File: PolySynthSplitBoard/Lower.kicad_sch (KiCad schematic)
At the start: 3 parts, among them J901 A_LOWER, J902 B_LOWER, J903 C_LOWER

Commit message: lower board
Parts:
- added J904: D_LOWER, Connector_PinSocket_2.54mm:PinSocket_1x03_P2.54mm_Vertical, symbol Connector:Conn_01x03_Pin
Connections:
- net GND: now also J904.1 (Pin_1)
- new net VOL_A: J904.2 (Pin_2)
- new net VOL_W: J904.3 (Pin_3)
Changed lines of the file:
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@@
+	(wire
+		(pts
+			(xy 148.59 127.508) (xy 145.542 127.508)
+		)
+		(stroke
+			(width 0)
+			(type default)
+		)
+	)
 	(wire
 		(pts
@@
 	(wire
 		(pts
+			(xy 148.59 128.524) (xy 148.59 127.508)
+		)
+		(stroke
+			(width 0)
+			(type default)
+		)
+	)
+	(wire
+		(pts
+			(xy 145.034 131.064) (xy 148.59 131.064)
+		)
+		(stroke
+			(width 0)
+			(type default)
+		)
+	)
+	(wire
+		(pts
 			(xy 85.852 131.064) (xy 85.852 130.048)
 		)
@@
 		(pts
 			(xy 84.582 146.304) (xy 85.852 146.304)
+		)
+		(stroke
+			(width 0)
+			(type default)
+		)
+	)
+	(wire
+		(pts
+			(xy 145.034 133.604) (xy 148.59 133.604)
 		)
 		(stroke
@@
 	(rectangle
 		(start 24.384 113.538)
-		(end 137.414 159.258)
+		(end 163.322 159.258)
 		(stroke
 			(width 0)
@@
 		)
 	)
+	(global_label "VOL_A"
+		(shape input)
+		(at 145.034 131.064 180)
+		(fields_autoplaced yes)
+		(effects
+			(font
+				(size 1.27 1.27)
+			)
+			(justify right)
+		)
+		(property "Intersheetrefs" "${INTERSHEET_REFS}"
+			(at 136.5454 131.064 0)
+			(effects
+				(font
+					(size 1.27 1.27)
+				)
+				(justify right)
+				(hide yes)
+			)
+		)
+	)
 	(global_label "EXP_MOSI"
 		(shape input)
@@
 		(property "Intersheetrefs" "${INTERSHEET_REFS}"
 			(at 71.4368 146.304 0)
+			(effects
+				(font
+					(size 1.27 1.27)
+				)
+				(justify right)
+				(hide yes)
+			)
+		)
+	)
+	(global_label "VOL_W"
+		(shape input)
+		(at 145.034 133.604 180)
+		(fields_autoplaced yes)
+		(effects
+			(font
+				(size 1.27 1.27)
+			)
+			(justify right)
+		)
+		(property "Intersheetrefs" "${INTERSHEET_REFS}"
+			(at 136.1826 133.604 0)
 			(effects
 				(font
@@
 				(path "/22649217-9810-470f-bc7b-6f743ad2b90e/3d9ecb3b-9556-42d6-955a-a32d9efd5d3a"
 					(reference "#PWR0902")
+					(unit 1)
+				)
+			)
+		)
+	)
+	(symbol
+		(lib_id "Connector:Conn_01x03_Pin")
+		(at 153.67 131.064 0)
+		(mirror y)
+		(unit 1)
+		(exclude_from_sim no)
+		(in_bom yes)
+		(on_board yes)
+		(dnp no)
+		(property "Reference" "J904"
+			(at 153.035 123.19 0)
+			(effects
+				(font
+					(size 1.27 1.27)
+				)
+			)
+		)
+		(property "Value" "D_LOWER"
+			(at 153.035 125.73 0)
+			(effects
+				(font
+					(size 1.27 1.27)
+				)
+			)
+		)
+		(property "Footprint" "Connector_PinSocket_2.54mm:PinSocket_1x03_P2.54mm_Vertical"
+			(at 153.67 131.064 0)
+			(effects
+				(font
+					(size 1.27 1.27)
+				)
+				(hide yes)
+			)
+		)
+		(property "Datasheet" "~"
+			(at 153.67 131.064 0)
+			(effects
+				(font
+					(size 1.27 1.27)
+				)
+				(hide yes)
+			)
+		)
+		(property "Description" "Generic connector, single row, 01x03, script generated"
+			(at 153.67 131.064 0)
+			(effects
+				(font
+					(size 1.27 1.27)
+				)
+				(hide yes)
+			)
+		)
+		(pin "2"
+		)
+		(pin "1"
+		)
+		(pin "3"
+		)
+		(instances
+			(project ""
+				(path "/22649217-9810-470f-bc7b-6f743ad2b90e/3d9ecb3b-9556-42d6-955a-a32d9efd5d3a"
+					(reference "J904")
 					(unit 1)
 				)
@@
 					(unit 1)
 				)
+			)
+		)
+	)
+	(symbol
+		(lib_id "power:GND")
+		(at 145.542 127.508 0)
+		(unit 1)
+		(exclude_from_sim no)
+		(in_bom yes)
+		(on_board yes)
+		(dnp no)
+		(fields_autoplaced yes)
+		(property "Reference" "#PWR0907"
+			(at 145.542 133.858 0)
+			(effects
+				(font
+					(size 1.27 1.27)
+				)
+				(hide yes)
+			)
+		)
+		(property "Value" "GND"
+			(at 145.542 131.318 0)
+			(effects
+				(font
+					(size 1.27 1.27)
+				)
+				(hide yes)
+			)
+		)
+		(property "Footprint" ""
+			(at 145.542 127.508 0)
+			(effects
+				(font
+					(size 1.27 1.27)
+				)
+				(hide yes)
+			)
+		)
+		(property "Datasheet" ""
+			(at 145.542 127.508 0)
+			(effects
+				(font
+					(size 1.27 1.27)
+				)
+				(hide yes)
+			)
+		)
+		(property "Description" ""
+			(at 145.542 127.508 0)
+			(effects
+				(font
+					(size 1.27 1.27)
+				)
+				(hide yes)
+			)
+		)
+		(pin "1"
+		)
+		(instances
+			(project "PolySynthSplitBoard"
+				(path "/22649217-9810-470f-bc7b-6f743ad2b90e/3d9ecb3b-9556-42d6-955a-a32d9efd5d3a"
+					(reference "#PWR0907")
+					(unit 1)
+				)

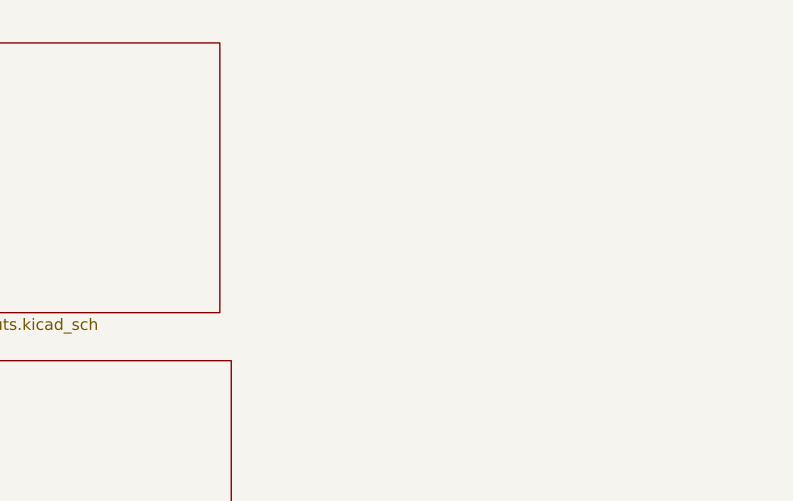
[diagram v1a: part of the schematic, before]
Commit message: hardware chip select for pitch registers
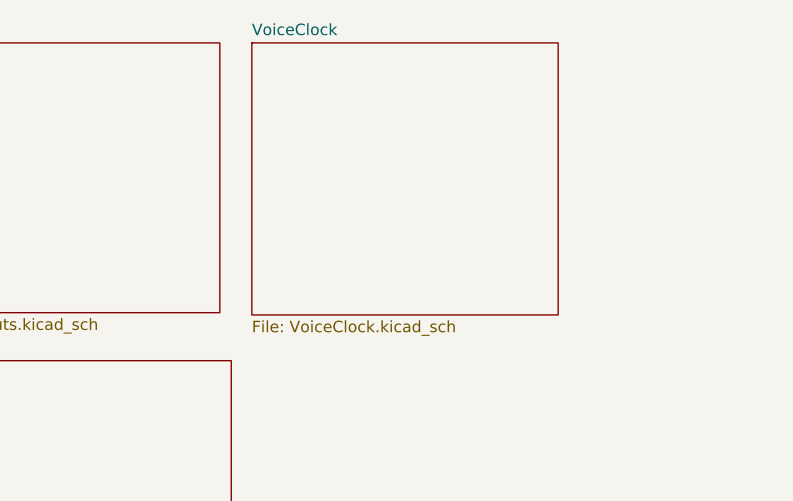
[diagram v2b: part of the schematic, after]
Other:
- added sheet VoiceClock (VoiceClock.kicad_sch)
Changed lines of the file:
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@@
+	)
+	(sheet
+		(at 105.156 22.606)
+		(size 34.036 30.226)
+		(fields_autoplaced yes)
+		(stroke
+			(width 0.1524)
+			(type solid)
+		)
+		(fill
+			(color 0 0 0 0.0000)
+		)
+		(property "Sheetname" "VoiceClock"
+			(at 105.156 21.8944 0)
+			(effects
+				(font
+					(size 1.27 1.27)
+				)
+				(justify left bottom)
+			)
+		)
+		(property "Sheetfile" "VoiceClock.kicad_sch"
+			(at 105.156 53.4166 0)
+			(effects
+				(font
+					(size 1.27 1.27)
+				)
+				(justify left top)
+			)
+		)
+		(instances
+			(project "PolySynthSplitBoard"
+				(path "/22649217-9810-470f-bc7b-6f743ad2b90e/3d9ecb3b-9556-42d6-955a-a32d9efd5d3a"
+					(page "10")
+				)
+			)
+		)
 	)
 	(sheet
